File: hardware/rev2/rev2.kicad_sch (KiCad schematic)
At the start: 46 parts, among them J1 USB_C_Receptacle_USB2.0_16P, J2 uFL, J3 uFL, J4 Antenna RF and GNSS Data, J5 Antenna GND, J7 uFL, U1 EClamp2522P

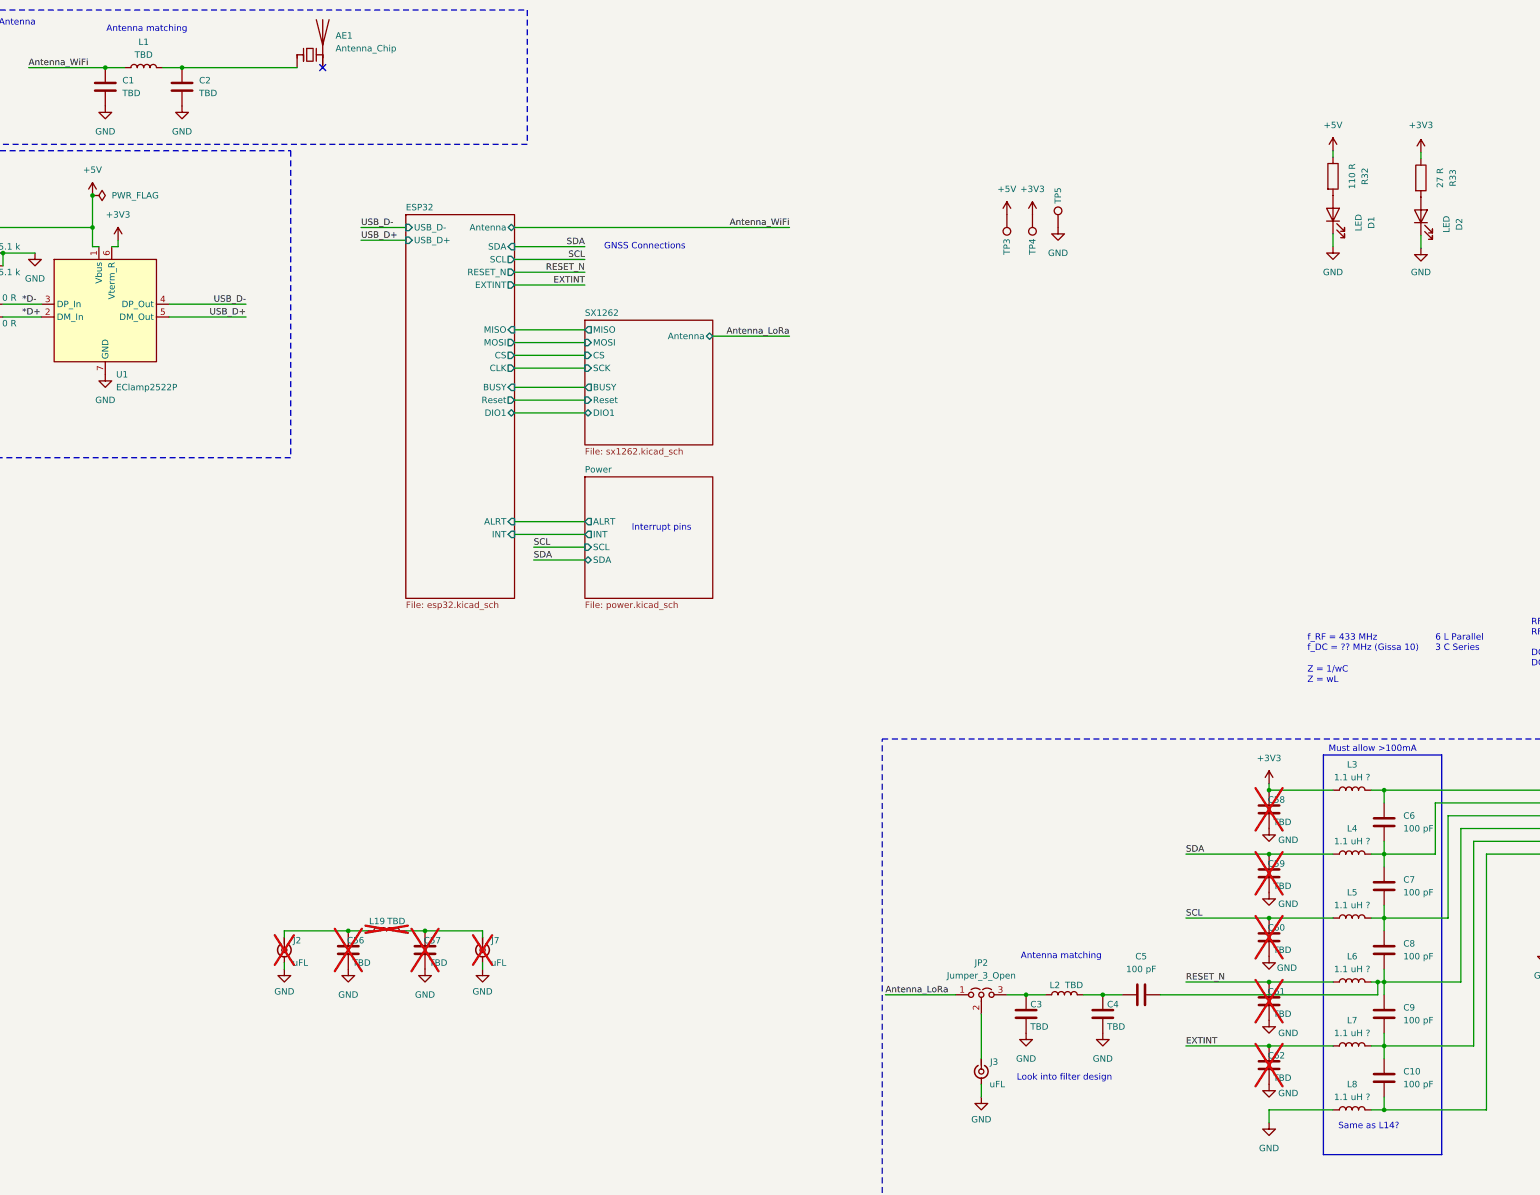
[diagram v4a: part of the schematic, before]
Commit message: fixed soldermask and silkscreen mostly
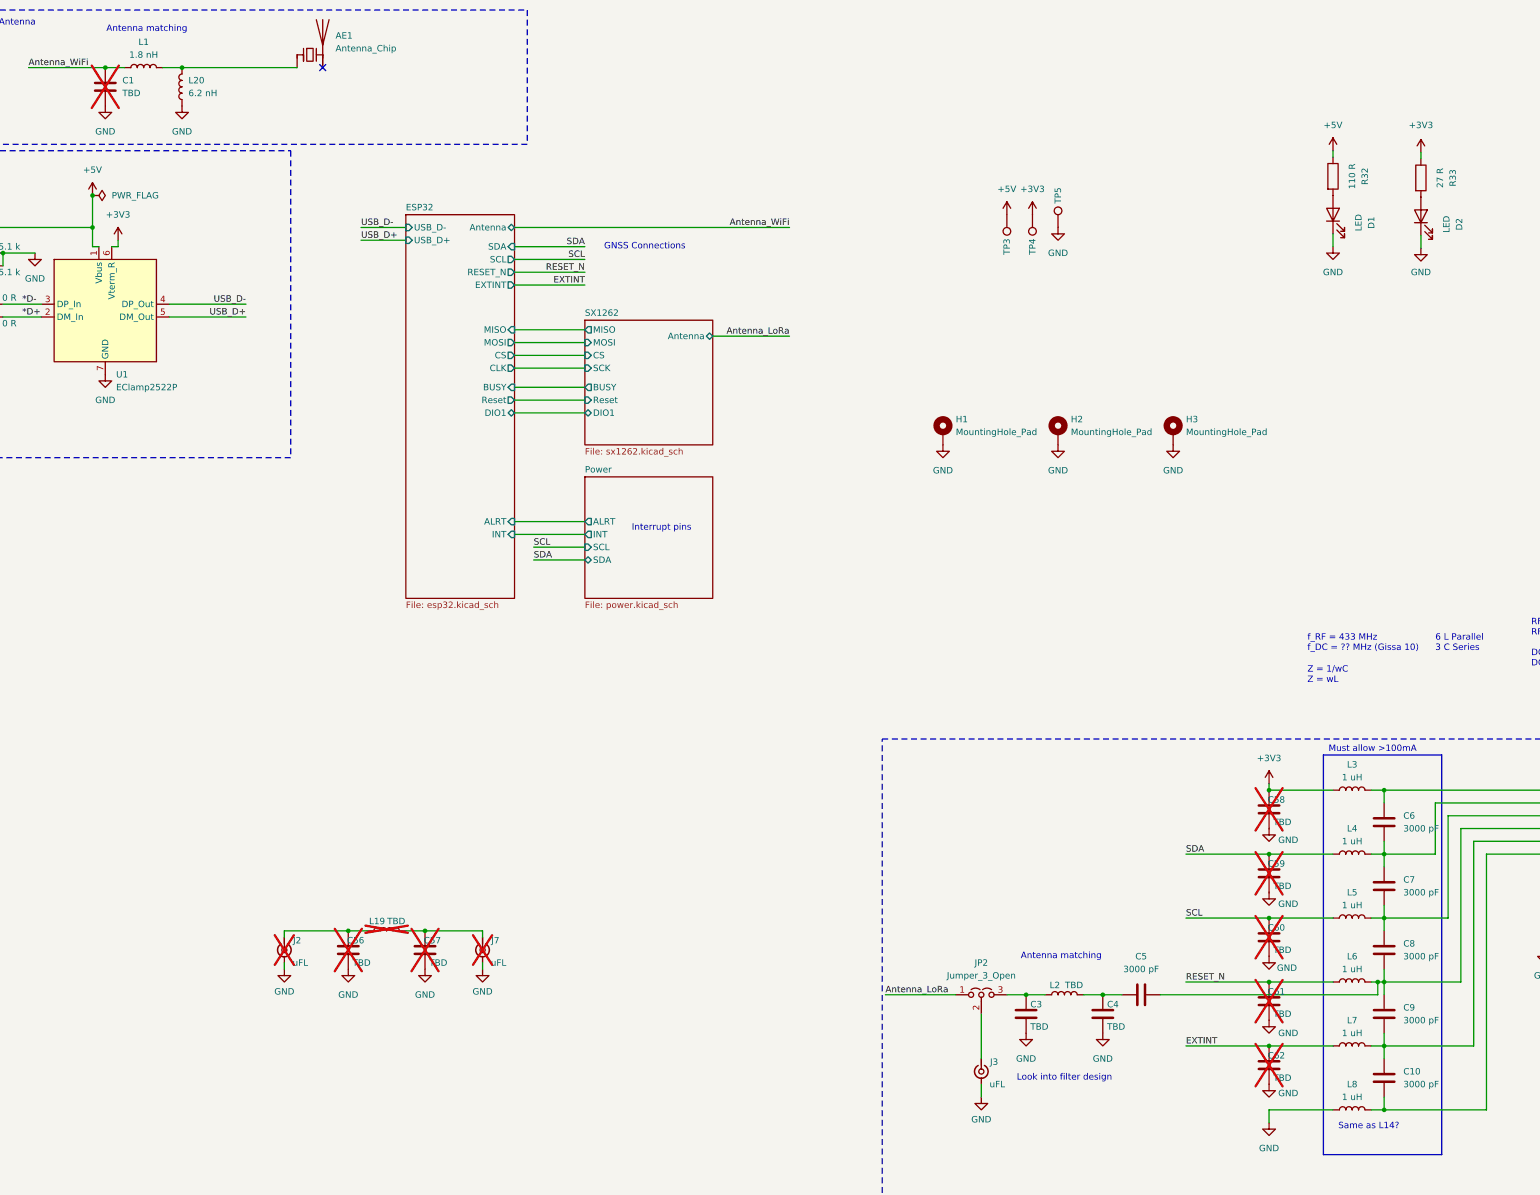
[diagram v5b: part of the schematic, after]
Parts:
- removed C2: TBD, Capacitor_SMD:C_0402_1005Metric_Pad0.74x0.62mm_HandSolder, symbol Device:C
- added H1, H2, H3: MountingHole_Pad, MountingHole:MountingHole_2.2mm_M2_Pad, symbol Mechanical:MountingHole_Pad
- added L20: 6.2 nH, Inductor_SMD:L_0402_1005Metric_Pad0.77x0.64mm_HandSolder, symbol Device:L
- C1: now not fitted; now left out of the parts list
- C10, C5, C6, C7, C8, C9: value 100 pF -> 3000 pF; Mouser Part Number (none) -> 81-GRM1557U1A302JA1D
- J4: Mouser Part Number 910-CQ-ESD-10 -> 910-CQ-ESD-14
- J5: Mouser Part Number (none) -> 855-M50-1900005
- JP2: Mouser Part Number (none) -> 71-CRCW04020000Z0EDC; now in the parts list
- L1: value TBD -> 1.8 nH; Mouser Part Number (none) -> 81-LQG15WH1N8C02D
- L3, L4, L5, L6, L7, L8: value 1.1 uH ? -> 1 uH; Mouser Part Number (none) -> 81-LQW15CA1R0K00D
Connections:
- net GND: now also H1.1, H2.1, H3.1, L20.2
- net at AE1.1 (FEED), L1.1: now also L20.1

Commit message: final edit, send to production
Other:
- company: MMCX11 -> Group 10
- title: (none) -> LoRa Based Cat Tracker
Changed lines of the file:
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@@
 	(paper "A3")
 	(title_block
-		(company "MMCX11")
+		(title "LoRa Based Cat Tracker")
+		(date "2026-04-22")
+		(rev "2.0.0")
+		(company "Group 10")
+		(comment 1 "MMCX11")
 	)
 	(rectangle
@@
 	(rectangle
 		(start 233.045 158.75)
-		(end 402.59 258.445)
+		(end 402.59 250.825)
 		(stroke
 			(width 0)

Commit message: changed some components that were on backorder
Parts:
- J2, J3, J7: Mouser Part Number 712-CONMHF1-SMD-G-T -> 712-CONUFL001-SMD-T
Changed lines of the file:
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@@
 			)
 		)
-		(property "Datasheet" "https://www.te.com/commerce/DocumentDelivery/DDEController?Action=srchrtrv&DocNm=conmhf1-smd-g-t-ds&DocType=Data+Sheet&DocLang=English&DocFormat=pdf&PartCntxt=CONMHF1-SMD-G-T"
+		(property "Datasheet" "https://www.te.com/commerce/DocumentDelivery/DDEController?Action=srchrtrv&DocNm=CONUFL001-SMD-T&DocType=Data+Sheet&DocLang=English&DocFormat=pdf&PartCntxt=CONUFL001-SMD-T"
 			(at 114.3 200.66 0)
 			(hide yes)
@@
 			)
 		)
-		(property "Mouser Part Number" "712-CONMHF1-SMD-G-T "
+		(property "Mouser Part Number" "712-CONUFL001-SMD-T "
 			(at 114.3 200.66 90)
 			(hide yes)
@@
 			)
 		)
-		(property "Datasheet" "https://www.te.com/commerce/DocumentDelivery/DDEController?Action=srchrtrv&DocNm=conmhf1-smd-g-t-ds&DocType=Data+Sheet&DocLang=English&DocFormat=pdf&PartCntxt=CONMHF1-SMD-G-T"
+		(property "Datasheet" "https://www.te.com/commerce/DocumentDelivery/DDEController?Action=srchrtrv&DocNm=CONUFL001-SMD-T&DocType=Data+Sheet&DocLang=English&DocFormat=pdf&PartCntxt=CONUFL001-SMD-T"
 			(at 252.73 224.79 0)
 			(hide yes)
@@
 			)
 		)
-		(property "Mouser Part Number" "712-CONMHF1-SMD-G-T "
+		(property "Mouser Part Number" "712-CONUFL001-SMD-T "
 			(at 252.73 224.79 90)
 			(hide yes)
@@
 			)
 		)
-		(property "Datasheet" "https://www.te.com/commerce/DocumentDelivery/DDEController?Action=srchrtrv&DocNm=conmhf1-smd-g-t-ds&DocType=Data+Sheet&DocLang=English&DocFormat=pdf&PartCntxt=CONMHF1-SMD-G-T"
+		(property "Datasheet" "https://www.te.com/commerce/DocumentDelivery/DDEController?Action=srchrtrv&DocNm=CONUFL001-SMD-T&DocType=Data+Sheet&DocLang=English&DocFormat=pdf&PartCntxt=CONUFL001-SMD-T"
 			(at 153.67 200.66 0)
 			(hide yes)
@@
 			)
 		)
-		(property "Mouser Part Number" "712-CONMHF1-SMD-G-T "
+		(property "Mouser Part Number" "712-CONUFL001-SMD-T "
 			(at 153.67 200.66 90)
 			(hide yes)

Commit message: tidied up some schematics
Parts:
- H1, H2, H3: value MountingHole_Pad -> Mounting Hole
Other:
- note added: "Footprints for testing"
- note added: "LoRa Antenna & Matching"
- note added: "Main Block Connections"
- note added: "Rail testpoints and LEDs"
- note removed: "GNSS Connections"
- note removed: "Look into filter design"
- note removed: "Must allow >100mA"
- note removed: "Ribbon cable goes here -->"
- note removed: "Same as L14?"
- moved on the sheet: C10, C3, C4, C5, C56, C57, C58, C59, C6, C60, C61, C62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
